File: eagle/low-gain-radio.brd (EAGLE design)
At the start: 99 x 100 mm, 109 parts, among them Y1 32MHz

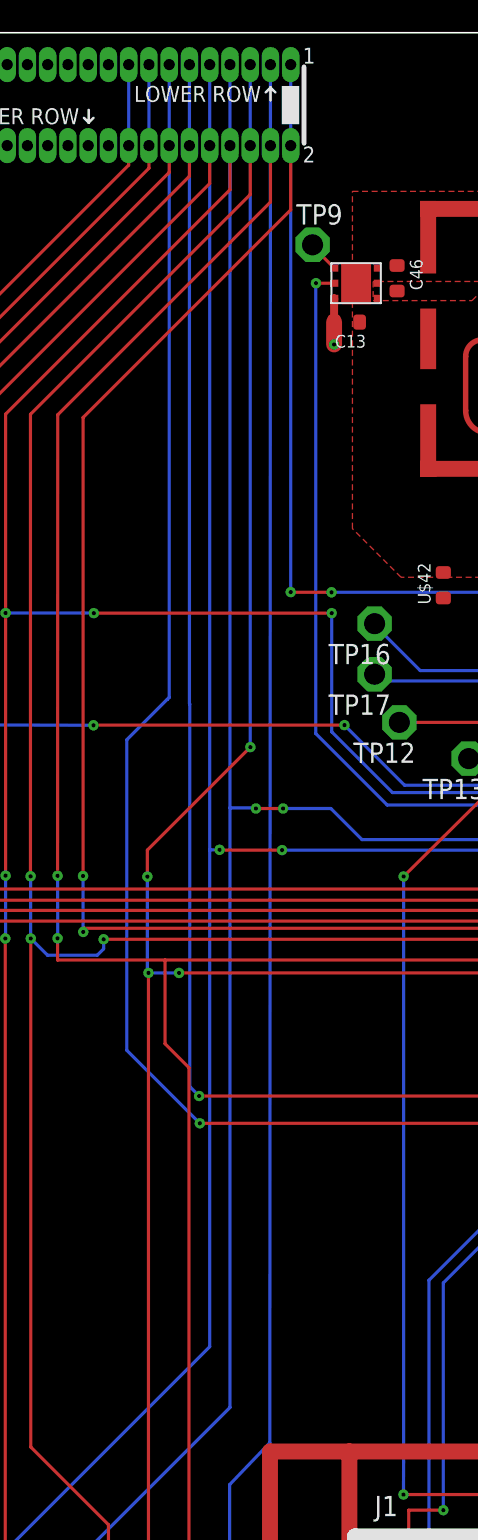
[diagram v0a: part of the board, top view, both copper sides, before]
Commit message: Updated pinout trace lines to fix DRC
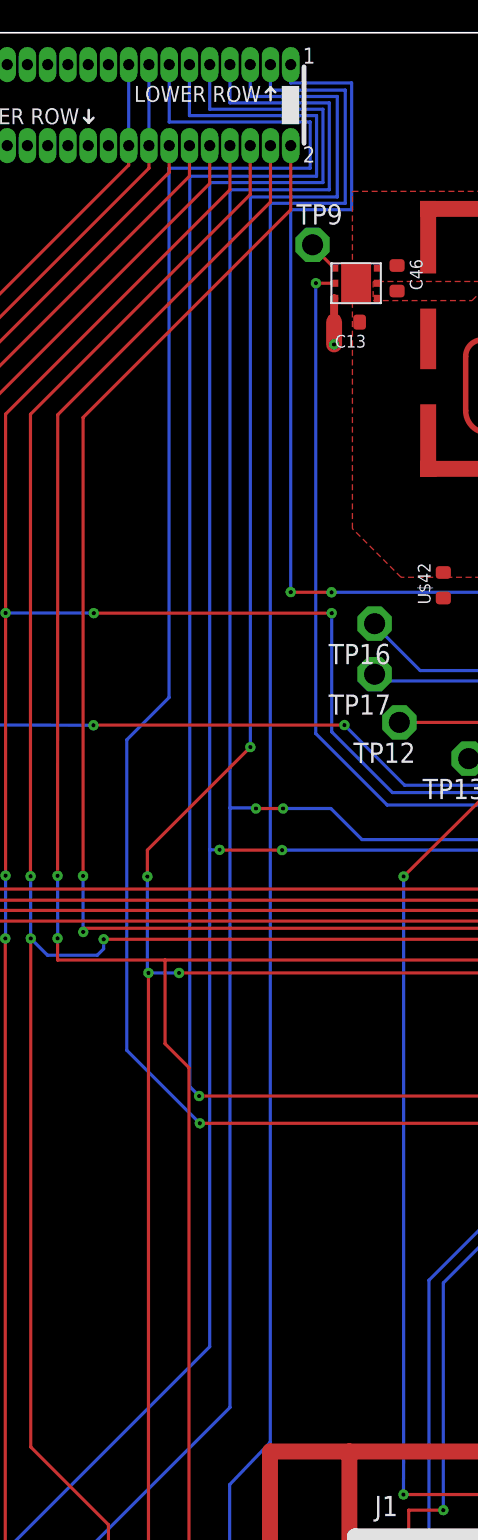
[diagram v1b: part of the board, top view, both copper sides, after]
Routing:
- net PTE18: track 120.5 -> 138.1 mm
- net PTE16: track 113.4 -> 129.3 mm
- net PTC7: track 164.1 -> 178.3 mm
- net PTC5: track 157.1 -> 169.5 mm
- net PTC3: track 218.7 -> 229.6 mm
- net PTC1: track 213.6 -> 223.0 mm
- net PTB2: track 84.5 -> 92.2 mm
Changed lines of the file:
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@@
 <?xml version="1.0" encoding="utf-8"?>
 <!DOCTYPE eagle SYSTEM "eagle.dtd">
-<eagle version="7.3.0">
+<eagle version="7.4.0">
 <drawing>
 <settings>
@@
 <layer number="13" name="Route13" color="4" fill="5" visible="no" active="no"/>
 <layer number="14" name="Route14" color="1" fill="6" visible="no" active="no"/>
-<layer number="15" name="Route15" color="14" fill="1" visible="no" active="yes"/>
+<layer number="15" name="Route15" color="14" fill="1" visible="yes" active="yes"/>
 <layer number="16" name="Bottom" color="1" fill="1" visible="yes" active="yes"/>
 <layer number="17" name="Pads" color="2" fill="1" visible="yes" active="yes"/>
@@
 <contactref element="KW0X" pad="21"/>
 <contactref element="CF1" pad="P$1"/>
-<wire x1="42.13" y1="98" x2="42.13" y2="64.92" width="0.2" layer="16"/>
 <wire x1="79.966171875" y1="58.055025" x2="84.07" y2="58.055025" width="0.2" layer="1"/>
 <wire x1="84.07" y1="58.055025" x2="84.07" y2="57.85" width="0.2" layer="1"/>
@@
 <wire x1="42.13" y1="64.91" x2="42.13" y2="64.92" width="0.2" layer="1"/>
 <via x="42.13" y="64.92" extent="1-16" drill="0.254"/>
+<wire x1="42.13" y1="98" x2="42.13" y2="96.85" width="0.2" layer="16"/>
+<wire x1="42.13" y1="96.85" x2="45.95" y2="96.85" width="0.2" layer="16"/>
+<wire x1="45.95" y1="96.85" x2="45.95" y2="88.9" width="0.2" layer="16"/>
+<wire x1="42.13" y1="64.92" x2="42.13" y2="88.9" width="0.2" layer="16"/>
+<wire x1="42.13" y1="88.9" x2="45.95" y2="88.9" width="0.2" layer="16"/>
 </signal>
 <signal name="PTB17">
@@
 <contactref element="R9" pad="2"/>
 <wire x1="79.966171875" y1="59.555025" x2="86.51" y2="59.555025" width="0.2" layer="1"/>
-<wire x1="40.86" y1="98" x2="40.82" y2="11.58" width="0.2" layer="16"/>
 <wire x1="40.82" y1="11.58" x2="38.3" y2="8.95" width="0.2" layer="16"/>
 <wire x1="38.3" y1="8.95" x2="38.3" y2="3.61" width="0.2" layer="16"/>
@@
 <wire x1="72.93" y1="0.67" x2="38.29" y2="0.67" width="0.2" layer="16"/>
 <wire x1="38.29" y1="0.67" x2="38.29" y2="3.6" width="0.2" layer="16"/>
+<wire x1="40.86" y1="98" x2="40.86" y2="96.4" width="0.2" layer="16"/>
+<wire x1="40.86" y1="96.4" x2="45.55" y2="96.4" width="0.2" layer="16"/>
+<wire x1="45.55" y1="96.4" x2="45.55" y2="89.3" width="0.2" layer="16"/>
+<wire x1="45.55" y1="89.3" x2="40.85" y2="89.3" width="0.2" layer="16"/>
+<wire x1="40.85" y1="89.3" x2="40.85" y2="11.58" width="0.2" layer="16"/>
+<wire x1="40.85" y1="11.58" x2="40.82" y2="11.58" width="0.2" layer="16"/>
 </signal>
 <signal name="PTC2">
@@
 <contactref element="CF1" pad="P$5"/>
 <contactref element="R11" pad="2"/>
-<wire x1="39.59" y1="98" x2="39.59" y2="55.21" width="0.2" layer="16"/>
 <wire x1="39.59" y1="55.21" x2="39.6" y2="55.2" width="0.2" layer="16"/>
 <via x="39.6" y="55.2" extent="1-16" drill="0.254"/>
@@
 <wire x1="33.14" y1="48.74" x2="39.6" y2="55.2" width="0.2" layer="1"/>
 <wire x1="33.21" y1="41.04" x2="35.13" y2="41.04" width="0.2" layer="16"/>
+<wire x1="39.59" y1="98" x2="39.59" y2="96" width="0.2" layer="16"/>
+<wire x1="39.59" y1="96" x2="45.05" y2="96" width="0.2" layer="16"/>
+<wire x1="45.05" y1="96" x2="45.05" y2="89.7" width="0.2" layer="16"/>
+<wire x1="45.05" y1="89.7" x2="39.6" y2="89.7" width="0.2" layer="16"/>
+<wire x1="39.6" y1="89.7" x2="39.6" y2="55.2" width="0.2" layer="16"/>
 </signal>
 <signal name="PTC4">
@@
 <wire x1="82.11" y1="53.85" x2="82.11" y2="49.39" width="0.2" layer="16"/>
 <wire x1="38.32" y1="13.79" x2="38.32" y2="51.389259375" width="0.2" layer="16"/>
-<wire x1="38.32" y1="51.389259375" x2="38.32" y2="98" width="0.2" layer="16"/>
 <wire x1="28.13" y1="3.6" x2="38.32" y2="13.79" width="0.2" layer="16"/>
 <wire x1="38.32" y1="51.389259375" x2="39.910740625" y2="51.389259375" width="0.2" layer="16"/>
@@
 <wire x1="78.85" y1="60.055025" x2="79.05" y2="59.855025" width="0.2" layer="1"/>
 <wire x1="79.05" y1="59.855025" x2="79.05" y2="59.3" width="0.2" layer="1"/>
+<wire x1="38.32" y1="98" x2="38.32" y2="95.6" width="0.2" layer="16"/>
+<wire x1="38.32" y1="95.6" x2="44.55" y2="95.6" width="0.2" layer="16"/>
+<wire x1="44.55" y1="95.6" x2="44.55" y2="90.15" width="0.2" layer="16"/>
+<wire x1="38.32" y1="51.389259375" x2="38.32" y2="90.15" width="0.2" layer="16"/>
+<wire x1="38.32" y1="90.15" x2="44.55" y2="90.15" width="0.2" layer="16"/>
 </signal>
 <signal name="PTC6">
@@
 <contactref element="KW0X" pad="5"/>
 <contactref element="CF1" pad="P$11"/>
-<wire x1="35.78" y1="98" x2="35.78" y2="57.92" width="0.2" layer="16"/>
-<wire x1="35.78" y1="57.92" x2="35.8" y2="57.9" width="0.2" layer="16"/>
 <wire x1="74.838371875" y1="54.427225" x2="74.838371875" y2="52.348371875" width="0.2" layer="1"/>
 <wire x1="35.8" y1="33.91" x2="36.39" y2="33.32" width="0.2" layer="16"/>
@@
 <via x="70.7" y="48.12" extent="1-16" drill="0.254"/>
 <wire x1="70.75" y1="48.26" x2="74.838371875" y2="52.348371875" width="0.2" layer="1"/>
-<wire x1="35.8" y1="33.91" x2="35.8" y2="57.9" width="0.2" layer="16"/>
 <wire x1="70.75" y1="48.26" x2="70.7" y2="48.26" width="0.2" layer="1"/>
 <wire x1="70.7" y1="48.26" x2="70.7" y2="48.12" width="0.2" layer="1"/>
+<wire x1="35.78" y1="98" x2="35.78" y2="94.8" width="0.2" layer="16"/>
+<wire x1="35.78" y1="94.8" x2="43.75" y2="94.8" width="0.2" layer="16"/>
+<wire x1="43.75" y1="94.8" x2="43.75" y2="91" width="0.2" layer="16"/>
+<wire x1="35.8" y1="33.91" x2="35.8" y2="91" width="0.2" layer="16"/>
+<wire x1="35.8" y1="91" x2="43.75" y2="91" width="0.2" layer="16"/>
 </signal>
 <signal name="PTE17">
@@
 <contactref element="KW0X" pad="7"/>
 <contactref element="CF1" pad="P$13"/>
-<wire x1="34.51" y1="98" x2="34.51" y2="58.31" width="0.2" layer="16"/>
-<wire x1="34.51" y1="58.31" x2="34.4" y2="58.2" width="0.2" layer="16"/>
 <wire x1="75.838371875" y1="54.427225" x2="75.838371875" y2="50.818371875" width="0.2" layer="1"/>
 <wire x1="75.838371875" y1="50.818371875" x2="73.13" y2="48.11" width="0.2" layer="1"/>
@@
 <wire x1="36.43" y1="31.61" x2="31.85" y2="36.19" width="0.2" layer="16"/>
 <wire x1="31.85" y1="36.19" x2="31.85" y2="55.66" width="0.2" layer="16"/>
-<wire x1="31.85" y1="55.66" x2="34.39" y2="58.2" width="0.2" layer="16"/>
-<wire x1="34.39" y1="58.2" x2="34.4" y2="58.2" width="0.2" layer="16"/>
+<wire x1="34.51" y1="98" x2="34.51" y2="94.4" width="0.2" layer="16"/>
+<wire x1="34.51" y1="94.4" x2="43.35" y2="94.4" width="0.2" layer="16"/>
+<wire x1="43.35" y1="94.4" x2="43.35" y2="91.5" width="0.2" layer="16"/>
+<wire x1="43.35" y1="91.5" x2="34.5" y2="91.5" width="0.2" layer="16"/>
+<wire x1="34.5" y1="91.5" x2="34.5" y2="58.31" width="0.2" layer="16"/>
+<wire x1="34.5" y1="58.31" x2="31.85" y2="55.66" width="0.2" layer="16"/>
 </signal>
 <signal name="PTE19">
@@
 <wire x1="23.05" y1="3.6" x2="37.05" y2="17.6" width="0.2" layer="16"/>
 <wire x1="37.05" y1="17.6" x2="37.05" y2="48.76" width="0.2" layer="16"/>
-<wire x1="37.05" y1="48.76" x2="37.05" y2="98" width="0.2" layer="16"/>
 <via x="77.08" y="59.22" extent="1-16" drill="0.254"/>
 <wire x1="37.05" y1="48.76" x2="37.67" y2="48.76" width="0.2" layer="16"/>
@@
 <wire x1="77.8" y1="59.94" x2="77.08" y2="59.22" width="0.2" layer="1"/>
 <wire x1="77.08" y1="59.22" x2="77.58" y2="59.72" width="0.2" layer="16"/>
+<wire x1="37.05" y1="98" x2="37.05" y2="95.2" width="0.2" layer="16"/>
+<wire x1="37.05" y1="95.2" x2="44.15" y2="95.2" width="0.2" layer="16"/>
+<wire x1="44.15" y1="95.2" x2="44.15" y2="90.6" width="0.2" layer="16"/>
+<wire x1="44.15" y1="90.6" x2="37.05" y2="90.6" width="0.2" layer="16"/>
+<wire x1="37.05" y1="90.6" x2="37.05" y2="48.76" width="0.2" layer="16"/>
 </signal>
 <signal name="N$3">
